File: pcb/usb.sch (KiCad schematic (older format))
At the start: 18 parts, among them J600 USB_B_Micro, U100 MCIMX7S5EVM08SC, U600 USBLC6-2SC6

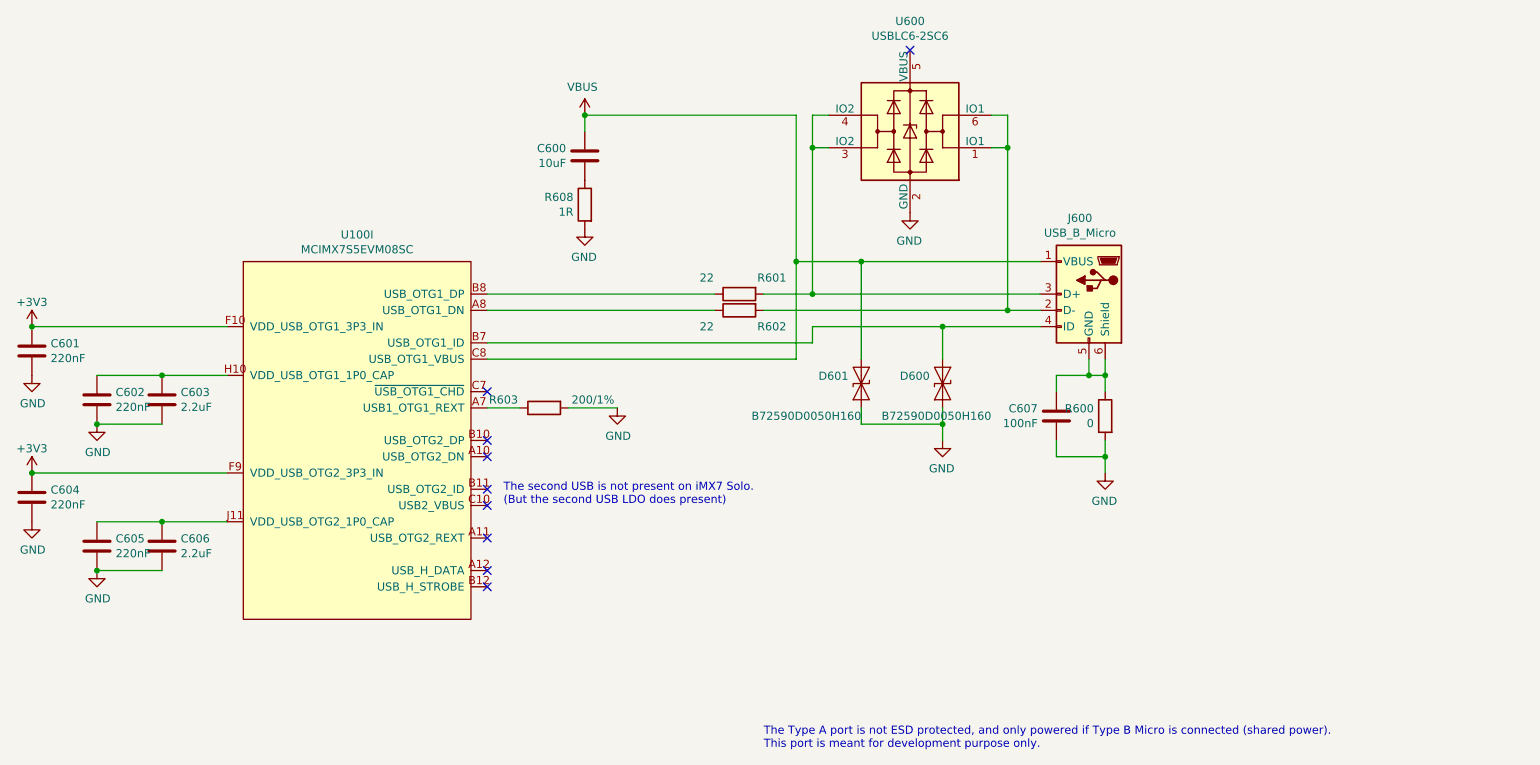
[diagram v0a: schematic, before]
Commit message: pcb: adding lpc5500
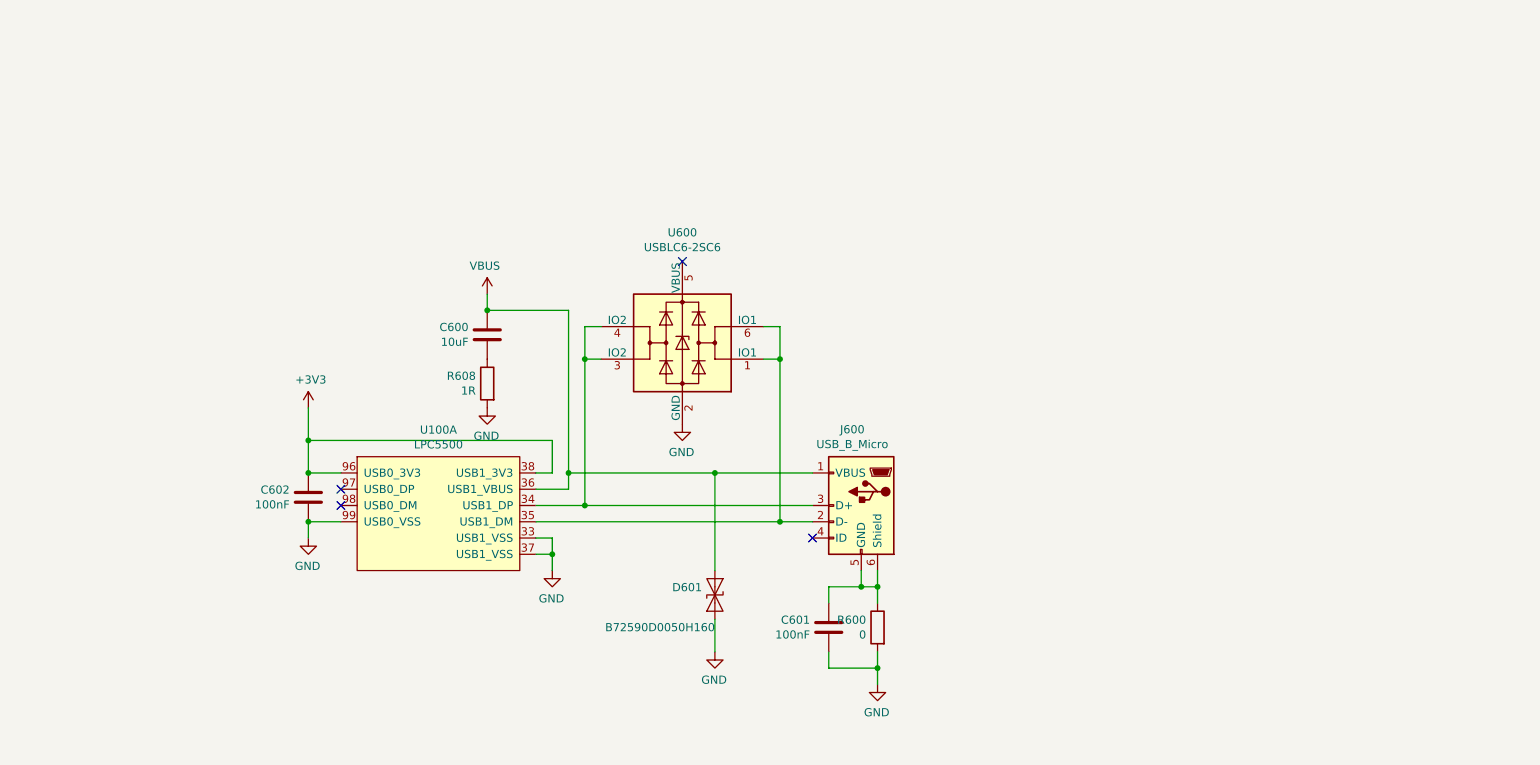
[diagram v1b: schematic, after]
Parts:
- removed C601, C604, C605: 220nF, Capacitor_SMD:C_0402_1005Metric, symbol Device:C
- removed C603, C606: 2.2uF, Capacitor_SMD:C_0402_1005Metric, symbol Device:C
- removed D600: B72590D0050H160, Diode_SMD:D_0402_1005Metric, symbol Device:D_TVS
- removed R601, R602: 22, Resistor_SMD:R_0603_1608Metric, symbol Device:R
- removed R603: 200/1%, Resistor_SMD:R_0603_1608Metric, symbol Device:R
- removed U100: MCIMX7S5EVM08SC, footprints:BGA-541_25x25_19.0x19.0mm, symbol symbols:MCIMX7S5EVM08SC
- added U100: LPC5500, Package_QFP:TQFP-100-1EP_14x14mm_P0.5mm_EP5x5mm_ThermalVias, symbol symbols:LPC5500
- C602: value 220nF -> 100nF
- renumbered C607 to C601
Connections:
- net +3V3: now also C602.1, U100.38 (USB1_3V3), U100.96 (USB0_3V3)
- net GND: now also U100.33 (USB1_VSS), U100.37 (USB1_VSS), U100.99 (USB0_VSS)
- net VBUS: now also U100.36 (USB1_VBUS)
- net at J600.2 (D-), U600.1 (IO1), U600.6 (IO1): now also U100.35 (USB1_DM)
- net at J600.3 (D+), U600.3 (IO2), U600.4 (IO2): now also U100.34 (USB1_DP)
- no-connect marks 9 -> 4
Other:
- note removed: "The Type A port is not ESD protected, and only powered if Type B Micro is connected (shared power). \nThis port is meant for development purpose only."
- note removed: "The second USB is not present on iMX7 Solo.\n(But the second USB LDO does present)"
- moved on the sheet: C600, C601, D601, J600, R600, R608, U600

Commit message: pcb: rev 0.1
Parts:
- added R601: 20K, Resistor_SMD:R_0603_1608Metric, symbol Device:R
- added R602: 10K, Resistor_SMD:R_0603_1608Metric, symbol Device:R
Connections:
- net GND: now also R601.1
- net VBUS: now also R602.1; no longer U100.36 (USB1_VBUS)
- net USB_DM: now reaches J600.2 (D-), U100.35 (USB1_DM), U600.1 (IO1), U600.6 (IO1)
- net USB_DP: now reaches J600.3 (D+), U100.34 (USB1_DP), U600.3 (IO2), U600.4 (IO2)
- new net: R601.2, R602.2, U100.36 (USB1_VBUS)
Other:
- moved on the sheet: C602, U100A
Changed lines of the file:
@@
 L power:GND #PWR0294
 U 1 1 5C99627A
-P 4200 4500
-F 0 "#PWR0294" H 4200 4250 50  0001 C CNN
-F 1 "GND" H 4205 4327 50  0000 C CNN
-F 2 "" H 4200 4500 50  0001 C CNN
-F 3 "" H 4200 4500 50  0001 C CNN
-	1    4200 4500
+P 3300 4500
+F 0 "#PWR0294" H 3300 4250 50  0001 C CNN
+F 1 "GND" H 3305 4327 50  0000 C CNN
+F 2 "" H 3300 4500 50  0001 C CNN
+F 3 "" H 3300 4500 50  0001 C CNN
+	1    3300 4500
 	-1   0    0    -1
 $EndComp
@@
 Connection ~ 7100 4400
 Wire Wire Line
-	7100 4400 5600 4400
-Wire Wire Line
 	7000 3400 7100 3400
 Connection ~ 7100 3400
@@
 	5900 3200 5900 3400
 Connection ~ 5900 4300
-Wire Wire Line
-	5900 4300 5600 4300
 Wire Wire Line
 	6000 3400 5900 3400
@@
 L symbols:LPC5500 U100
 U 1 1 5D749DD3
-P 5000 4300
-F 0 "U100" H 5000 4765 50  0000 C CNN
-F 1 "LPC5500" H 5000 4674 50  0000 C CNN
-F 2 "Package_QFP:TQFP-100-1EP_14x14mm_P0.5mm_EP5x5mm_ThermalVias" H 5000 4700 50  0001 C CNN
-F 3 "" H 4900 4350 50  0001 C CNN
-	1    5000 4300
+P 4100 4300
+F 0 "U100" H 4100 4765 50  0000 C CNN
+F 1 "LPC5500" H 4100 4674 50  0000 C CNN
+F 2 "Package_QFP:TQFP-100-1EP_14x14mm_P0.5mm_EP5x5mm_ThermalVias" H 4100 4700 50  0001 C CNN
+F 3 "" H 4000 4350 50  0001 C CNN
+	1    4100 4300
 	1    0    0    -1
 $EndComp
@@
 NoConn ~ 7300 4500
 $Comp
-L power:GND #PWR?
+L power:GND #PWR0153
 U 1 1 5D75956E
-P 5700 4700
-F 0 "#PWR?" H 5700 4450 50  0001 C CNN
-F 1 "GND" H 5705 4527 50  0000 C CNN
-F 2 "" H 5700 4700 50  0001 C CNN
-F 3 "" H 5700 4700 50  0001 C CNN
-	1    5700 4700
-	-1   0    0    -1
-$EndComp
-Wire Wire Line
-	5600 4500 5700 4500
-Wire Wire Line
-	5700 4500 5700 4600
-Wire Wire Line
-	5600 4600 5700 4600
-Connection ~ 5700 4600
-Wire Wire Line
-	5700 4600 5700 4700
+P 4800 4700
+F 0 "#PWR0153" H 4800 4450 50  0001 C CNN
+F 1 "GND" H 4805 4527 50  0000 C CNN
+F 2 "" H 4800 4700 50  0001 C CNN
+F 3 "" H 4800 4700 50  0001 C CNN
+	1    4800 4700
+	-1   0    0    -1
+$EndComp
+Wire Wire Line
+	4700 4500 4800 4500
+Wire Wire Line
+	4800 4500 4800 4600
+Wire Wire Line
+	4700 4600 4800 4600
+Connection ~ 4800 4600
+Wire Wire Line
+	4800 4600 4800 4700
 Wire Wire Line
 	5300 3100 5800 3100
@@
 Connection ~ 5300 3100
 Wire Wire Line
-	4200 4400 4200 4500
-NoConn ~ 4400 4200
-NoConn ~ 4400 4300
-$Comp
-L power:+3V3 #PWR?
+	3300 4400 3300 4500
+NoConn ~ 3500 4200
+NoConn ~ 3500 4300
+$Comp
+L power:+3V3 #PWR0154
 U 1 1 5D76C848
-P 4200 3700
-F 0 "#PWR?" H 4200 3550 50  0001 C CNN
-F 1 "+3V3" H 4215 3873 50  0000 C CNN
-F 2 "" H 4200 3700 50  0001 C CNN
-F 3 "" H 4200 3700 50  0001 C CNN
-	1    4200 3700
+P 3300 3700
+F 0 "#PWR0154" H 3300 3550 50  0001 C CNN
+F 1 "+3V3" H 3315 3873 50  0000 C CNN
+F 2 "" H 3300 3700 50  0001 C CNN
+F 3 "" H 3300 3700 50  0001 C CNN
+	1    3300 3700
 	1    0    0    -1
 $EndComp
 $Comp
-L power:GND #PWR?
+L power:GND #PWR0155
 U 1 1 5D76D29D
 P 5300 3700
-F 0 "#PWR?" H 5300 3450 50  0001 C CNN
+F 0 "#PWR0155" H 5300 3450 50  0001 C CNN
 F 1 "GND" H 5305 3527 50  0000 C CNN
 F 2 "" H 5300 3700 50  0001 C CNN
@@
 $EndComp
 Wire Wire Line
-	5600 4100 5700 4100
-Wire Wire Line
-	4200 3900 4200 4100
-Wire Wire Line
-	5700 3900 5700 4100
-Wire Wire Line
-	4200 3700 4200 3900
-Connection ~ 4200 3900
+	4700 4100 4800 4100
+Wire Wire Line
+	3300 3900 3300 4100
+Wire Wire Line
+	4800 3900 4800 4100
+Wire Wire Line
+	3300 3700 3300 3900
+Connection ~ 3300 3900
 $Comp
 L Device:C C602
 U 1 1 5D85A4D4
-P 4200 4250
-F 0 "C602" H 4315 4296 50  0000 L CNN
-F 1 "100nF" H 4315 4205 50  0000 L CNN
-F 2 "Capacitor_SMD:C_0402_1005Metric" H 4238 4100 50  0001 C CNN
-F 3 "~" H 4200 4250 50  0001 C CNN
-	1    4200 4250
-	-1   0    0    -1
-$EndComp
-Wire Wire Line
-	4200 4100 4400 4100
-Connection ~ 4200 4100
-Wire Wire Line
-	4200 4400 4400 4400
-Connection ~ 4200 4400
-Wire Wire Line
-	4200 3900 5700 3900
+P 3300 4250
+F 0 "C602" H 3415 4296 50  0000 L CNN
+F 1 "100nF" H 3415 4205 50  0000 L CNN
+F 2 "Capacitor_SMD:C_0402_1005Metric" H 3338 4100 50  0001 C CNN
+F 3 "~" H 3300 4250 50  0001 C CNN
+	1    3300 4250
+	-1   0    0    -1
+$EndComp
+Wire Wire Line
+	3300 4100 3500 4100
+Connection ~ 3300 4100
+Wire Wire Line
+	3300 4400 3500 4400
+Connection ~ 3300 4400
+Wire Wire Line
+	3300 3900 4800 3900
+Wire Wire Line
+	4700 4300 5900 4300
+Wire Wire Line
+	4700 4400 7100 4400
+Text Label 4900 4300 0    50   ~ 0
+USB_DP
+Text Label 4900 4400 0    50   ~ 0
+USB_DM
+$Comp
+L Device:R R602
+U 1 1 5D867F2F
+P 5450 4200
+F 0 "R602" V 5650 4100 50  0000 L CNN
+F 1 "10K" V 5550 4150 50  0000 L CNN
+F 2 "Resistor_SMD:R_0603_1608Metric" V 5380 4200 50  0001 C CNN
+F 3 "~" H 5450 4200 50  0001 C CNN
+	1    5450 4200
+	0    1    -1   0
+$EndComp
+$Comp
+L Device:R R601
+U 1 1 5D8690B6
+P 5300 4350
+F 0 "R601" H 5350 4500 50  0000 L CNN
+F 1 "20K" H 5350 4600 50  0000 L CNN
+F 2 "Resistor_SMD:R_0603_1608Metric" V 5230 4350 50  0001 C CNN
+F 3 "~" H 5300 4350 50  0001 C CNN
+	1    5300 4350
+	1    0    0    1
+$EndComp
+$Comp
+L power:GND #PWR0158
+U 1 1 5D869EE7
+P 5300 4500
+F 0 "#PWR0158" H 5300 4250 50  0001 C CNN
+F 1 "GND" H 5305 4327 50  0000 C CNN
+F 2 "" H 5300 4500 50  0001 C CNN
+F 3 "" H 5300 4500 50  0001 C CNN
+	1    5300 4500
+	-1   0    0    -1
+$EndComp
+Wire Wire Line
+	4700 4200 5300 4200
+Connection ~ 5300 4200
 $EndSCHEMATC
